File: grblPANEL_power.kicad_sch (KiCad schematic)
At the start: 24 parts, among them J101 Conn_01x02, U101 MAX17612A, U102 AZ1117-3.3

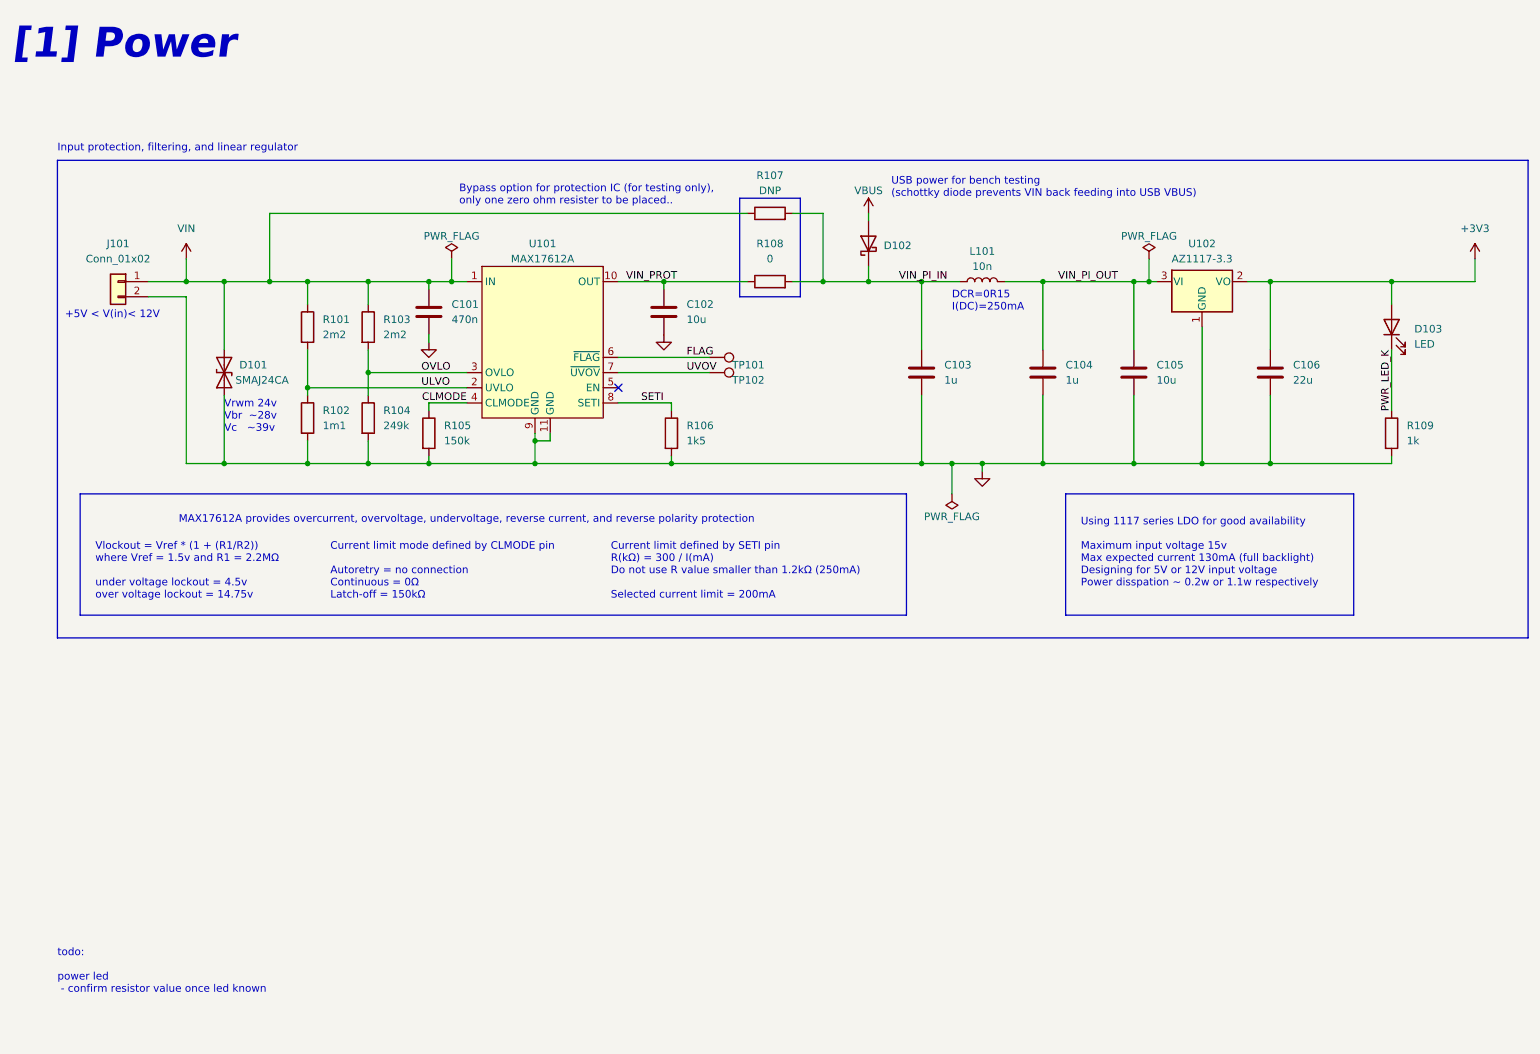
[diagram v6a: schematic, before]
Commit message: Add power protection status LEDs
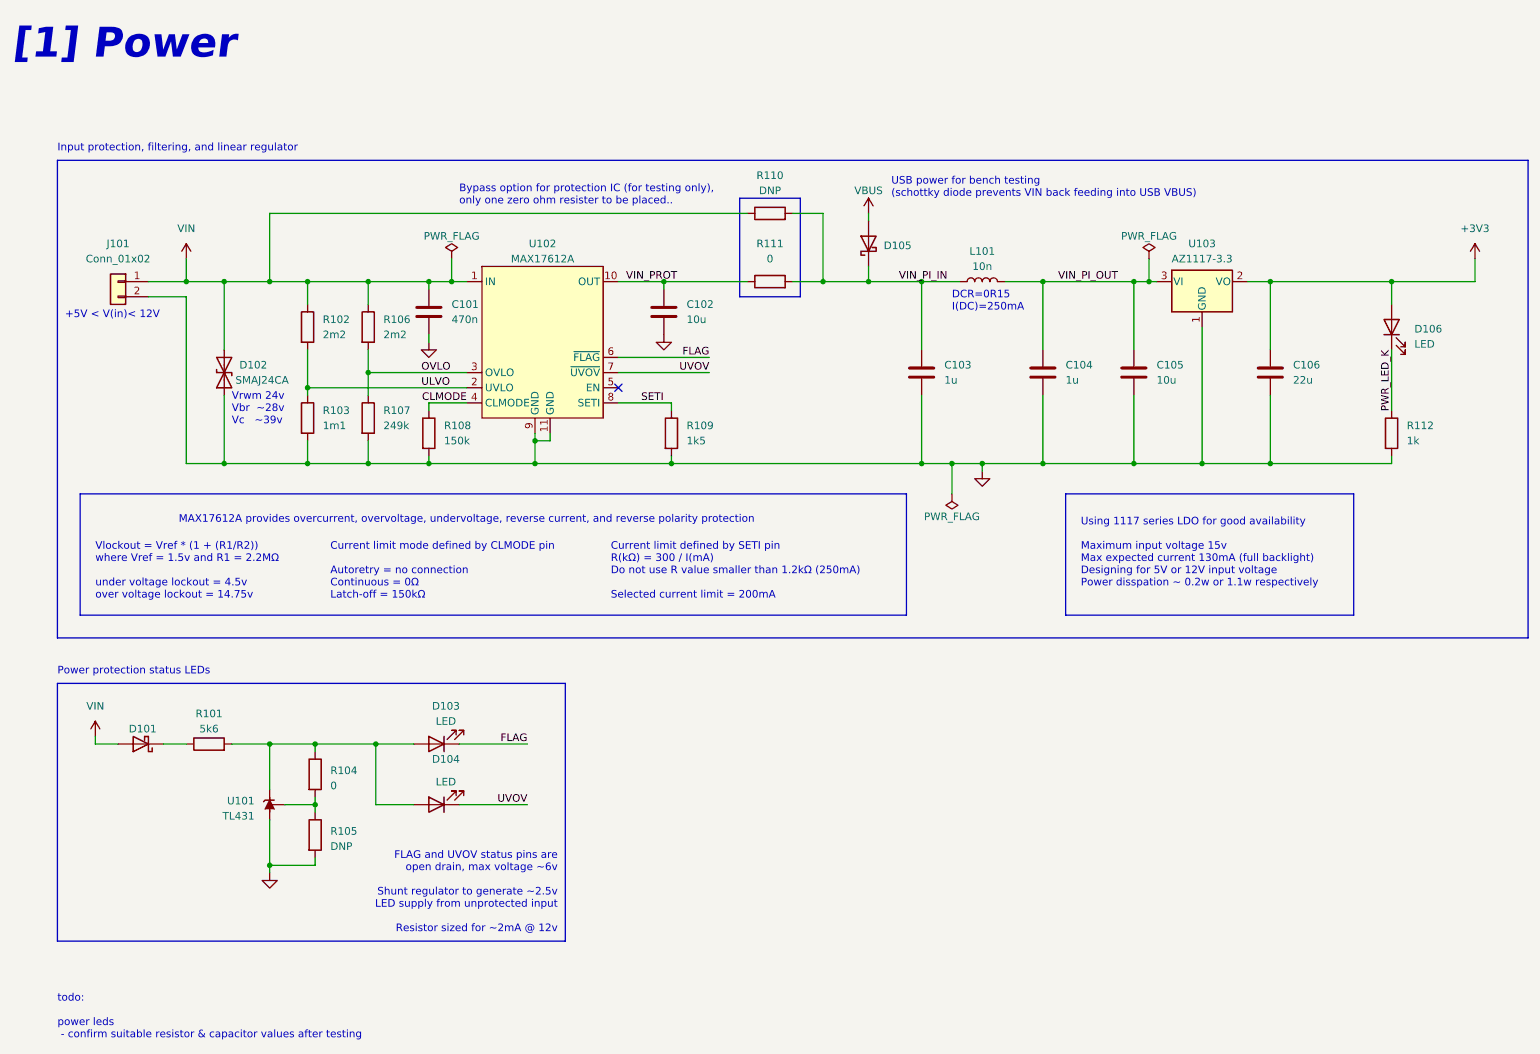
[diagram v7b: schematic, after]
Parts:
- removed TP101, TP102: TestPoint, TestPoint:TestPoint_THTPad_D2.0mm_Drill1.0mm, symbol Connector:TestPoint
- added D101: D_Schottky, Diode_SMD:D_SOD-323, symbol Device:D_Schottky
- added D103, D104: LED, LED_SMD:LED_1206_3216Metric_ReverseMount_Hole1.8x2.4mm, symbol Device:LED
- added R101: 5k6, Resistor_SMD:R_0603_1608Metric, symbol Device:R
- added R104: 0, Resistor_SMD:R_0603_1608Metric, symbol Device:R
- added R105: DNP, Resistor_SMD:R_0603_1608Metric, symbol Device:R
- added U101: TL431, Package_TO_SOT_SMD:SOT-23, symbol Reference_Voltage:TL431DBZ
- D106: renamed from D103; footprint LED_SMD:LED_0603_1608Metric -> LED_SMD:LED_1206_3216Metric_ReverseMount_Hole1.8x2.4mm
- renumbered D101 to D102, D102 to D105, R101 to R102, R102 to R103, R103 to R106, R104 to R107, R105 to R108, R106 to R109, R107 to R110, R108 to R111, R109 to R112, U101 to U102, U102 to U103
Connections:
- net FLAG: now also D103.1 (K)
- net GND: now also R105.2, U101.3 (A)
- net UVOV: now also D104.1 (K)
- net VIN: now also D101.2 (A)
- new net: D101.1 (K), R101.1
- new net: D103.2 (A), D104.2 (A), R101.2, R104.1, U101.1 (K)
- new net: R104.2, R105.1, U101.2 (REF)
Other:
- note added: "FLAG and UVOV status pins are open drain, max voltage ~6v Shunt regulator to generate ~2.5v LED supply from unprotected input Resistor sized for ~2mA @ 12v"
- note added: "Power protection status LEDs"
- note added: "todo: power leds - confirm suitable resistor & capacitor values after testing"
- note removed: "todo: power led - confirm resistor value once led known"

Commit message: Place and route changes from schematic
Headers for serial console.
DNP components to v7 format.
Power status components.
LEDs to bottom side, plus silkscreen.
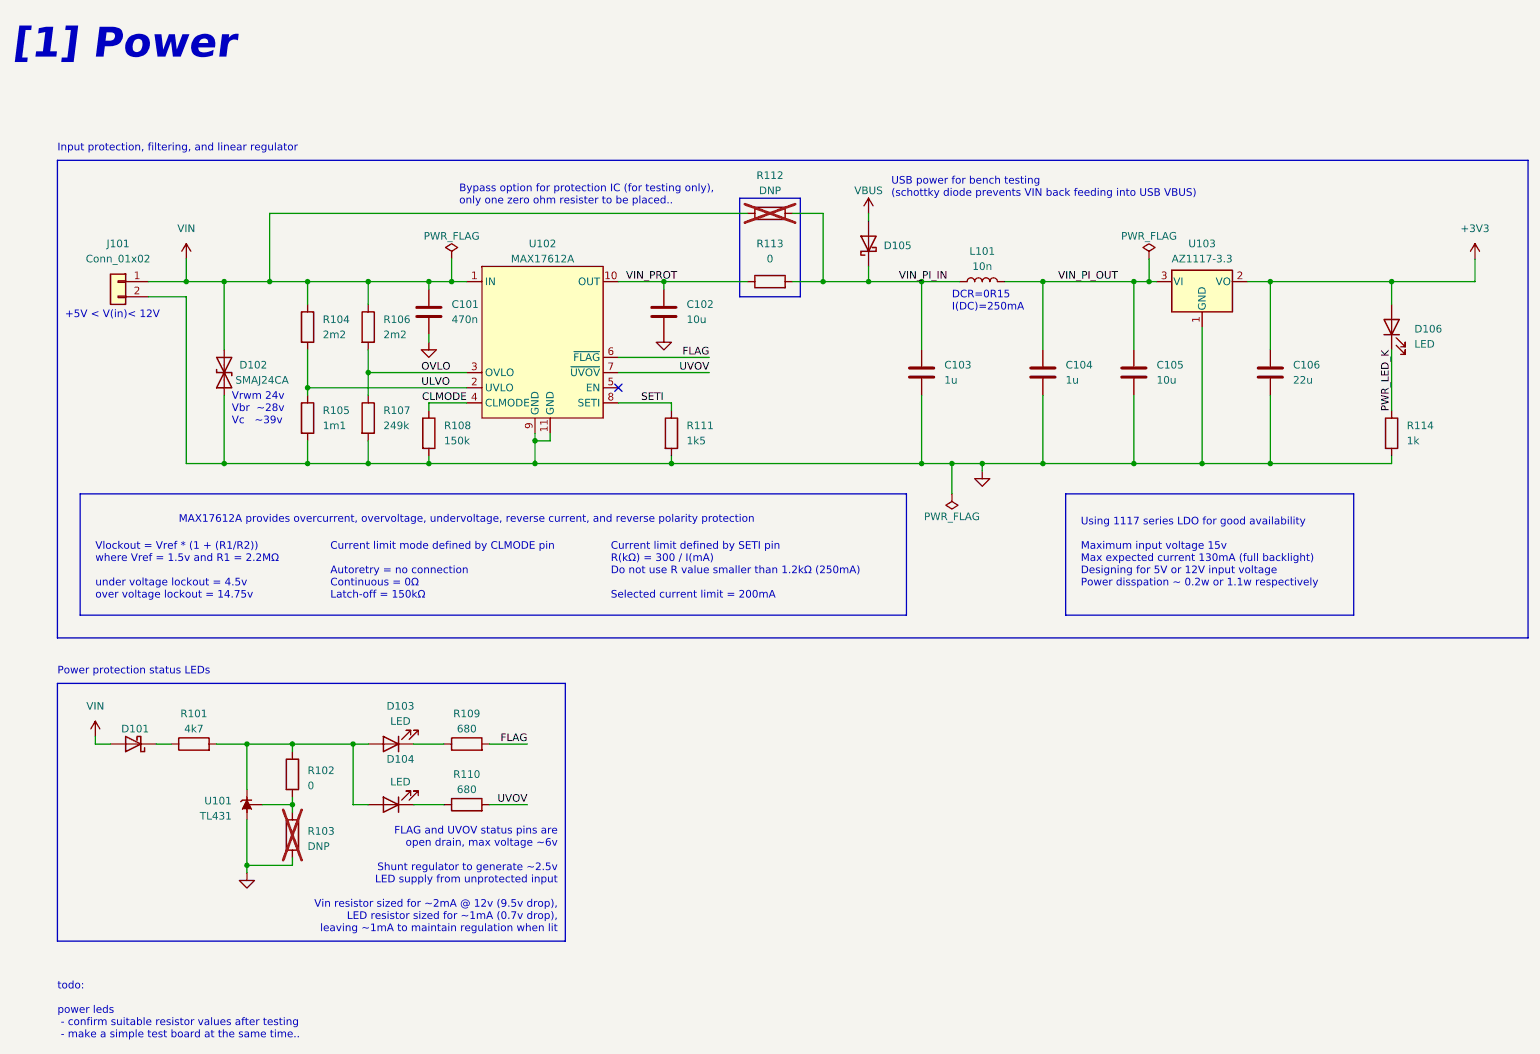
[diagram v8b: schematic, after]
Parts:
- added R109, R110: 680, Resistor_SMD:R_0603_1608Metric, symbol Device:R
- D103, D104, D106: footprint LED_SMD:LED_1206_3216Metric_ReverseMount_Hole1.8x2.4mm -> LED_SMD:LED_0603_1608Metric
- R101: value 5k6 -> 4k7
- R103: renamed from R105; now not fitted
- R112: renamed from R110; now not fitted
- renumbered R104 to R102, R102 to R104, R103 to R105, R109 to R111, R111 to R113, R112 to R114
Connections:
- net FLAG: now also R109.2; no longer D103.1 (K)
- net UVOV: now also R110.2; no longer D104.1 (K)
- new net: D104.1 (K), R110.1
- new net: D103.1 (K), R109.1
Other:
- note added: "FLAG and UVOV status pins are open drain, max voltage ~6v Shunt regulator to generate ~2.5v LED supply from unprotected input Vin resistor sized for ~2mA @ 12v (9.5v drop), LED resistor sized for ~1mA (0.7v drop), leaving ~1mA to maintain regulation when lit"
- note added: "todo: power leds - confirm suitable resistor values after testing - make a simple test board at the same time.."
- note removed: "FLAG and UVOV status pins are open drain, max voltage ~6v Shunt regulator to generate ~2.5v LED supply from unprotected input Resistor sized for ~2mA @ 12v"
- note removed: "todo: power leds - confirm suitable resistor & capacitor values after testing"
- moved on the sheet: D101, D103, D104, R101, R102, U101
